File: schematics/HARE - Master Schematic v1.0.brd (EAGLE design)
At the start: 105.1 x 80 mm, 93 parts, among them IC1 NE5532N, IC2 NE5532N, IC3 FT232RL, IC4 NE5532N, IC5 7805DT, IC6 AT25P, J1 9V, J2 STEREOSW, J3 STEREOSW, Q1 16 MHz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

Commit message: Updated master schematic
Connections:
- removed net V+: IC1.8
- removed net V-: IC1.4
- net GND: now also IC1.4
- net VCC: now also IC1.8
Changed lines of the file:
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@@
 <contactref element="C25" pad="2"/>
 <contactref element="R35" pad="2"/>
+<contactref element="IC1" pad="8"/>
 <wire x1="92.99" y1="73.66" x2="97.79" y2="76.66" width="0" layer="19" extent="1-1"/>
 <wire x1="102.87" y1="47.31" x2="92.99" y2="73.66" width="0" layer="19" extent="1-1"/>
@@
 <wire x1="54.229" y1="40.005" x2="74.549" y2="40.386" width="0" layer="19" extent="1-1"/>
 <wire x1="54.102" y1="44.77" x2="54.229" y2="40.005" width="0" layer="19" extent="1-1"/>
-<wire x1="17.51" y1="64.77" x2="54.102" y2="44.77" width="0" layer="19" extent="1-1"/>
-<wire x1="11.912" y1="58.426" x2="17.51" y2="64.77" width="0" layer="19" extent="1-1"/>
-<wire x1="35.88" y1="2.54" x2="54.229" y2="40.005" width="0" layer="19" extent="1-1"/>
+<wire x1="36.195" y1="40.005" x2="54.229" y2="40.005" width="0" layer="19" extent="1-1"/>
+<wire x1="11.912" y1="58.426" x2="36.195" y2="40.005" width="0" layer="19" extent="1-1"/>
+<wire x1="17.51" y1="64.77" x2="11.912" y2="58.426" width="0" layer="19" extent="1-1"/>
+<wire x1="35.88" y1="2.54" x2="36.195" y2="40.005" width="0" layer="19" extent="1-1"/>
 </signal>
 <signal name="GND">
@@
 <contactref element="U2" pad="7"/>
 <contactref element="U2" pad="5"/>
+<contactref element="IC1" pad="4"/>
 <wire x1="95.758" y1="60.706" x2="97.79" y2="70.66" width="0" layer="19" extent="1-1"/>
 <wire x1="95.758" y1="55.626" x2="95.758" y2="60.706" width="0" layer="19" extent="1-1"/>
@@
 <wire x1="17.78" y1="18.275" x2="11.43" y2="18.275" width="0" layer="19" extent="1-1"/>
 <wire x1="23.13" y1="19.05" x2="17.78" y2="18.275" width="0" layer="19" extent="1-1"/>
+<wire x1="43.815" y1="32.385" x2="33.226" y2="41.275" width="0" layer="19" extent="1-1"/>
+<wire x1="41.91" y1="27.94" x2="43.815" y2="32.385" width="0" layer="19" extent="1-1"/>
 <wire x1="29.718" y1="55.88" x2="33.226" y2="41.275" width="0" layer="19" extent="1-1"/>
 <wire x1="31.75" y1="59.69" x2="29.718" y2="55.88" width="0" layer="19" extent="1-1"/>
-<wire x1="41.91" y1="27.94" x2="33.226" y2="41.275" width="0" layer="19" extent="1-1"/>
 <wire x1="28.21" y1="3.81" x2="23.13" y2="19.05" width="0" layer="19" extent="1-1"/>
 <wire x1="17.78" y1="2.045" x2="28.21" y2="3.81" width="0" layer="19" extent="1-1"/>
 <wire x1="11.43" y1="2.045" x2="17.78" y2="2.045" width="0" layer="19" extent="1-1"/>
-<wire x1="53.34" y1="11.43" x2="41.91" y2="27.94" width="0" layer="19" extent="1-1"/>
-<wire x1="63.77" y1="22.86" x2="53.34" y2="11.43" width="0" layer="19" extent="1-1"/>
-<wire x1="61.849" y1="32.385" x2="63.77" y2="22.86" width="0" layer="19" extent="1-1"/>
+<wire x1="61.849" y1="32.385" x2="43.815" y2="32.385" width="0" layer="19" extent="1-1"/>
+<wire x1="63.77" y1="22.86" x2="61.849" y2="32.385" width="0" layer="19" extent="1-1"/>
+<wire x1="53.34" y1="11.43" x2="63.77" y2="22.86" width="0" layer="19" extent="1-1"/>
 <wire x1="80.01" y1="22.86" x2="63.77" y2="22.86" width="0" layer="19" extent="1-1"/>
 <wire x1="88.9" y1="19.545" x2="80.01" y2="22.86" width="0" layer="19" extent="1-1"/>
@@
 <contactref element="IC6" pad="7"/>
 </signal>
-<signal name="V+">
-<contactref element="IC1" pad="8"/>
-</signal>
-<signal name="V-">
-<contactref element="IC1" pad="4"/>
-</signal>
 <signal name="N$12">

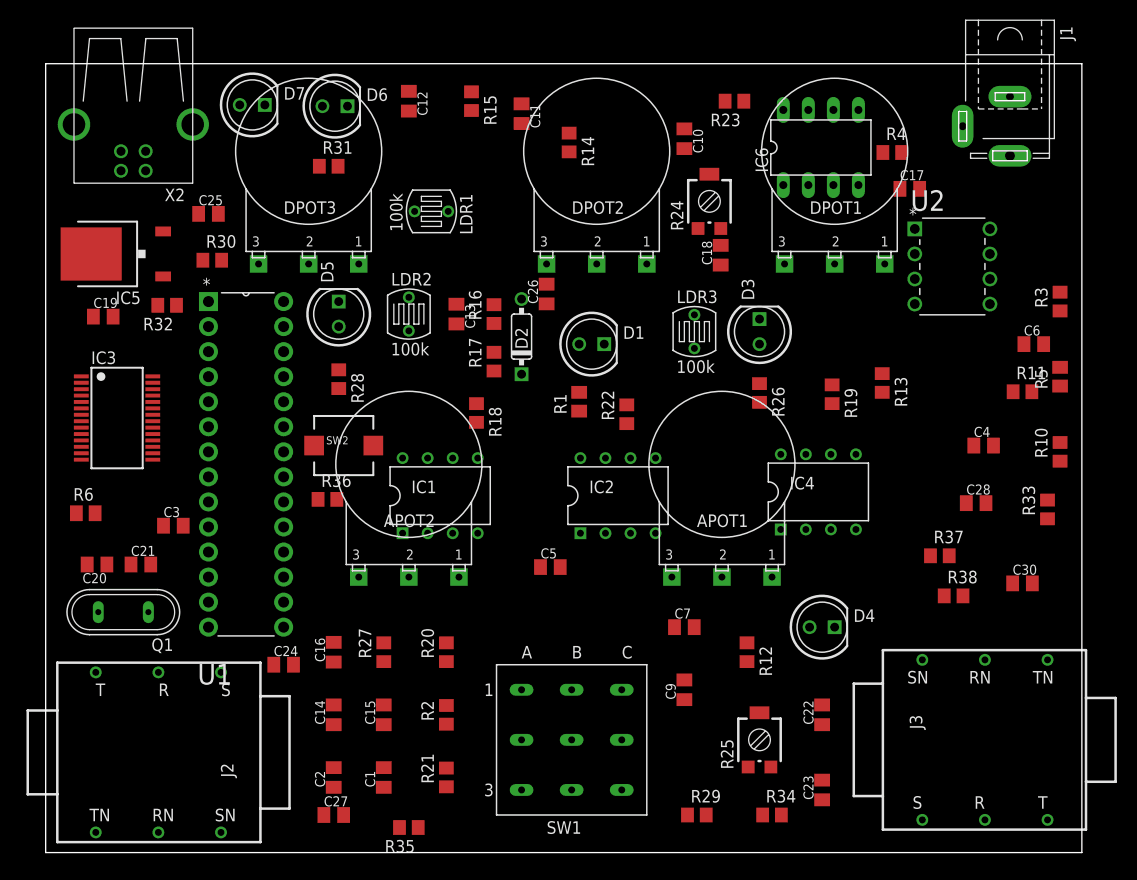
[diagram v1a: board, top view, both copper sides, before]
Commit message: Started the eagle layout and fixed a few errors in the schematic
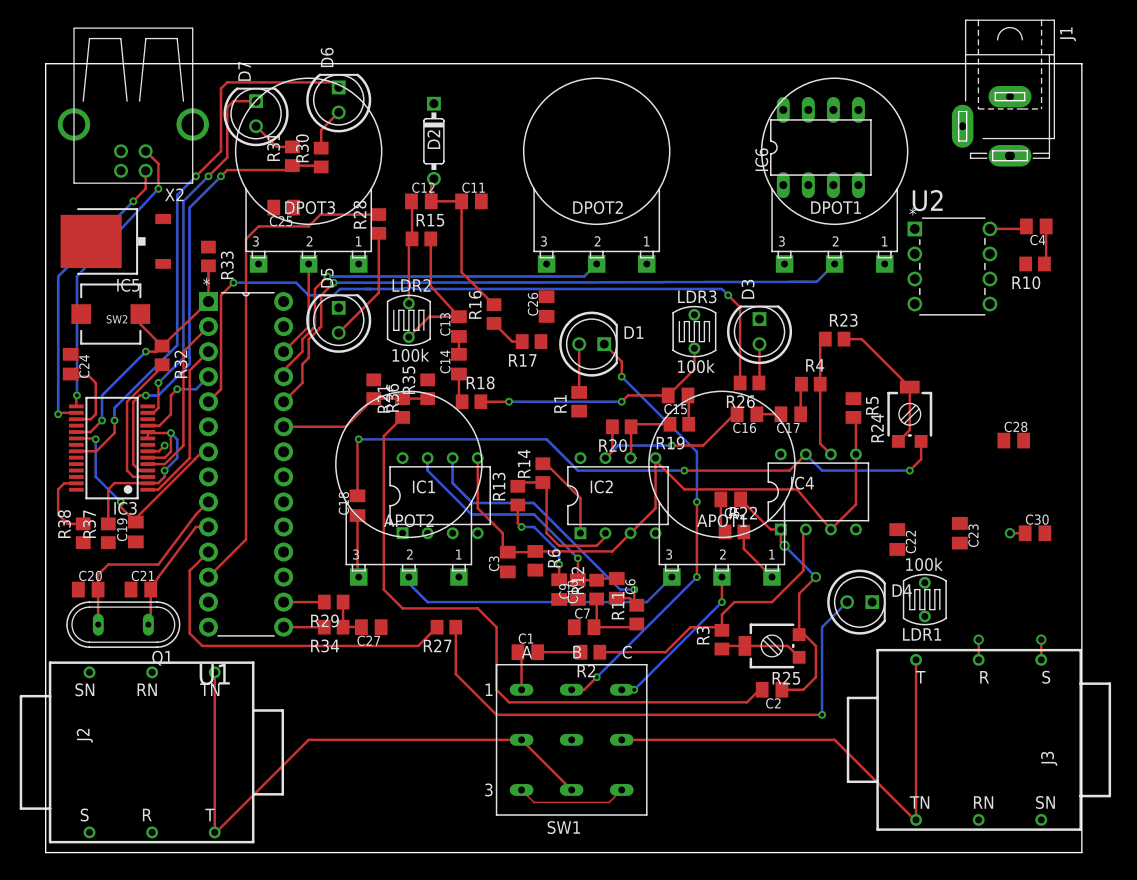
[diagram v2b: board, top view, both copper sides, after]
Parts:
- moved R33 88.9 mm to (16.5, 60.5), turned to 270 degrees
- moved R38 88.5 mm to (3.81, 32.4), turned to 90 degrees
- moved R37 84.4 mm to (6.35, 32.4), turned to 90 degrees
- moved LDR1 63.7 mm to (89.2, 25.7), turned to 180 degrees
- moved C6 49.0 mm to (57.9, 26.8), turned to 270 degrees
- moved R3 48.5 mm to (68.6, 21.6)
- moved C16 48.4 mm to (71.1, 44.5), turned to 180 degrees
- moved R34 48.4 mm to (29.2, 22.9), turned to 180 degrees
- moved C10 47.5 mm to (52.1, 26.7)
- moved R6 45.8 mm to (49.7, 29.6), turned to 270 degrees
- moved C2 45.3 mm to (73.7, 16.5), turned to 180 degrees
- moved R11 45.2 mm to (59.9, 24.1), turned to 90 degrees
- moved C18 44.7 mm to (31.6, 35.2)
- moved R35 44.5 mm to (38.7, 47.0), turned to 90 degrees
- moved C15 44.0 mm to (64.1, 46.4), turned to 180 degrees
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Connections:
- removed net N$47: APOT1.2, SW1.C2
- new net N$15: APOT1.2, SW1.C1
- net N$19: now also SW1.C2; no longer SW1.C1
- net N$36: now also C2.2
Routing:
- net N$60: track 0.00 -> 74.4 mm, vias 0 -> 2
- net N$43: track 0.00 -> 67.8 mm, vias 0 -> 3
- net V_BIAS: track 0.00 -> 66.5 mm
- net ADC1: track 0.00 -> 65.7 mm, vias 0 -> 1
- net N$36: track 0.00 -> 65.6 mm
- net INPUT: track 0.00 -> 58.4 mm
- net CBUS1: track 0.00 -> 56.5 mm, vias 0 -> 2
- net N$59: track 0.00 -> 56.1 mm, vias 0 -> 1
- net N$56: track 0.00 -> 50.4 mm
- net N$19: track 0.00 -> 49.4 mm
- net VCCIO: track 0.00 -> 46.5 mm, vias 0 -> 2
- net N$8: track 0.00 -> 44.9 mm, vias 0 -> 4
- net ADC2: track 0.00 -> 39.8 mm, vias 0 -> 1
- net CBUS2: track 0.00 -> 37.8 mm, vias 0 -> 2
- net N$58: track 0.00 -> 35.4 mm
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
